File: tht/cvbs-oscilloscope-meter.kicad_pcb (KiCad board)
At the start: 2 copper layers, 50 parts, among them J1 Conn_Coaxial_Power, J2 Conn_Coaxial_Power, J3 Conn_Coaxial_Power, J4 Conn_Coaxial_Power, J5 Barrel_Jack_Switch, J6 Molex 3.96mm, Q1 2N3906, Q2 2N3906, Q3 2N3904, Q4 2N3904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

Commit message: Updated THT
Starting new routing for new schematic layout
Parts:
- C6: footprint Inductor_THT:L_Axial_L11.0mm_D4.5mm_P15.24mm_Horizontal_Fastron_MECC -> Capacitor_THT:C_Disc_D7.5mm_W2.5mm_P5.00mm
- moved U1 91.6 mm to (167.5, 120.3)
- moved U2 33.4 mm to (197.3, 117.2)
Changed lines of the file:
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@@
     )
   )
-  (footprint "Inductor_THT:L_Axial_L11.0mm_D4.5mm_P15.24mm_Horizontal_Fastron_MECC" (layer "F.Cu")
+  (footprint "Capacitor_THT:C_Disc_D7.5mm_W2.5mm_P5.00mm" (layer "F.Cu")
     (at 151.57 102.68)
-    (descr "Inductor, Axial series, Axial, Horizontal, pin pitch=15.24mm, , length*diameter=11*4.5mm^2, Fastron, MECC, http://www.fastrongroup.com/image-show/21/MECC.pdf?type=Complete-DataSheet&productType=series")
-    (tags "Inductor Axial series Axial Horizontal pin pitch 15.24mm  length 11mm diameter 4.5mm Fastron MECC")
-    (property "Sheetfile" "cvbs-oscilloscope-meter.kicad_sch")
-    (property "Sheetname" "")
-    (attr through_hole)
-    (fp_text reference "C6" (at 7.62 -3.37) (layer "F.SilkS")
-      (effects (font (size 1 1) (thickness 0.15)))
-    )
-    (fp_text value "10u" (at 7.62 3.37) (layer "F.Fab")
-      (effects (font (size 1 1) (thickness 0.15)))
-    )
-    (fp_text user "${REFERENCE}" (at 7.62 0) (layer "F.Fab")
-      (effects (font (size 1 1) (thickness 0.15)))
-    )
-    (fp_line (start 13.24 2.37) (end 13.24 -2.37) (layer "F.SilkS") (width 0.12))
-    (fp_line (start 2 2.37) (end 13.24 2.37) (layer "F.SilkS") (width 0.12))
-    (fp_line (start 1.24 0) (end 2 0) (layer "F.SilkS") (width 0.12))
-    (fp_line (start 14 0) (end 13.24 0) (layer "F.SilkS") (width 0.12))
-    (fp_line (start 2 -2.37) (end 2 2.37) (layer "F.SilkS") (width 0.12))
-    (fp_line (start 13.24 -2.37) (end 2 -2.37) (layer "F.SilkS") (width 0.12))
-    (fp_line (start -1.25 2.5) (end 16.5 2.5) (layer "F.CrtYd") (width 0.05))
-    (fp_line (start 16.5 -2.5) (end -1.25 -2.5) (layer "F.CrtYd") (width 0.05))
-    (fp_line (start 16.5 2.5) (end 16.5 -2.5) (layer "F.CrtYd") (width 0.05))
-    (fp_line (start -1.25 -2.5) (end -1.25 2.5) (layer "F.CrtYd") (width 0.05))
-    (fp_line (start 13.12 -2.25) (end 2.12 -2.25) (layer "F.Fab") (width 0.1))
-    (fp_line (start 13.12 2.25) (end 13.12 -2.25) (layer "F.Fab") (width 0.1))
-    (fp_line (start 2.12 2.25) (end 13.12 2.25) (layer "F.Fab") (width 0.1))
-    (fp_line (start 0 0) (end 2.12 0) (layer "F.Fab") (width 0.1))
-    (fp_line (start 2.12 -2.25) (end 2.12 2.25) (layer "F.Fab") (width 0.1))
-    (fp_line (start 15.24 0) (end 13.12 0) (layer "F.Fab") (width 0.1))
+    (descr "C, Disc series, Radial, pin pitch=5.00mm, , diameter*width=7.5*2.5mm^2, Capacitor, http://www.vishay.com/docs/28535/vy2series.pdf")
+    (tags "C Disc series Radial pin pitch 5.00mm  diameter 7.5mm width 2.5mm Capacitor")
+    (property "Sheetfile" "cvbs-oscilloscope-meter.kicad_sch")
+    (property "Sheetname" "")
+    (attr through_hole)
+    (fp_text reference "C6" (at 2.5 -2.5) (layer "F.SilkS")
+      (effects (font (size 1 1) (thickness 0.15)))
+    )
+    (fp_text value "10u" (at 2.5 2.5) (layer "F.Fab")
+      (effects (font (size 1 1) (thickness 0.15)))
+    )
+    (fp_text user "${REFERENCE}" (at 2.5 0) (layer "F.Fab")
+      (effects (font (size 1 1) (thickness 0.15)))
+    )
+    (fp_line (start -1.37 1.37) (end 6.37 1.37) (layer "F.SilkS") (width 0.12))
+    (fp_line (start -1.37 -1.37) (end -1.37 1.37) (layer "F.SilkS") (width 0.12))
+    (fp_line (start 6.37 -1.37) (end 6.37 1.37) (layer "F.SilkS") (width 0.12))
+    (fp_line (start -1.37 -1.37) (end 6.37 -1.37) (layer "F.SilkS") (width 0.12))
+    (fp_line (start 6.5 -1.5) (end -1.5 -1.5) (layer "F.CrtYd") (width 0.05))
+    (fp_line (start -1.5 -1.5) (end -1.5 1.5) (layer "F.CrtYd") (width 0.05))
+    (fp_line (start 6.5 1.5) (end 6.5 -1.5) (layer "F.CrtYd") (width 0.05))
+    (fp_line (start -1.5 1.5) (end 6.5 1.5) (layer "F.CrtYd") (width 0.05))
+    (fp_line (start -1.25 -1.25) (end -1.25 1.25) (layer "F.Fab") (width 0.1))
+    (fp_line (start 6.25 1.25) (end 6.25 -1.25) (layer "F.Fab") (width 0.1))
+    (fp_line (start -1.25 1.25) (end 6.25 1.25) (layer "F.Fab") (width 0.1))
+    (fp_line (start 6.25 -1.25) (end -1.25 -1.25) (layer "F.Fab") (width 0.1))
     (pad "1" thru_hole circle (at 0 0) (size 2 2) (drill 1) (layers *.Cu *.Mask)
       (net 2 "+9V") (pintype "passive"))
-    (pad "2" thru_hole oval (at 15.24 0) (size 2 2) (drill 1) (layers *.Cu *.Mask)
+    (pad "2" thru_hole circle (at 5 0) (size 2 2) (drill 1) (layers *.Cu *.Mask)
       (net 6 "GND") (pintype "passive"))
-    (model "${KICAD6_3DMODEL_DIR}/Inductor_THT.3dshapes/L_Axial_L11.0mm_D4.5mm_P15.24mm_Horizontal_Fastron_MECC.wrl"
+    (model "${KICAD6_3DMODEL_DIR}/Capacitor_THT.3dshapes/C_Disc_D7.5mm_W2.5mm_P5.00mm.wrl"
       (offset (xyz 0 0 0))
       (scale (xyz 1 1 1))
@@
   )
   (footprint "Package_DIP:DIP-8_W7.62mm_Socket_LongPads" (layer "F.Cu")
-    (at 234.5 57.92)
+    (at 167.475 120.33)
     (descr "8-lead though-hole mounted DIP package, row spacing 7.62 mm (300 mils), Socket, LongPads")
     (tags "THT DIP DIL PDIP 2.54mm 7.62mm 300mil Socket LongPads")
@@
   )
   (footprint "Package_DIP:DIP-8_W7.62mm_Socket_LongPads" (layer "F.Cu")
-    (at 202.54 84.12)
+    (at 197.32 117.155)
     (descr "8-lead though-hole mounted DIP package, row spacing 7.62 mm (300 mils), Socket, LongPads")
     (tags "THT DIP DIL PDIP 2.54mm 7.62mm 300mil Socket LongPads")

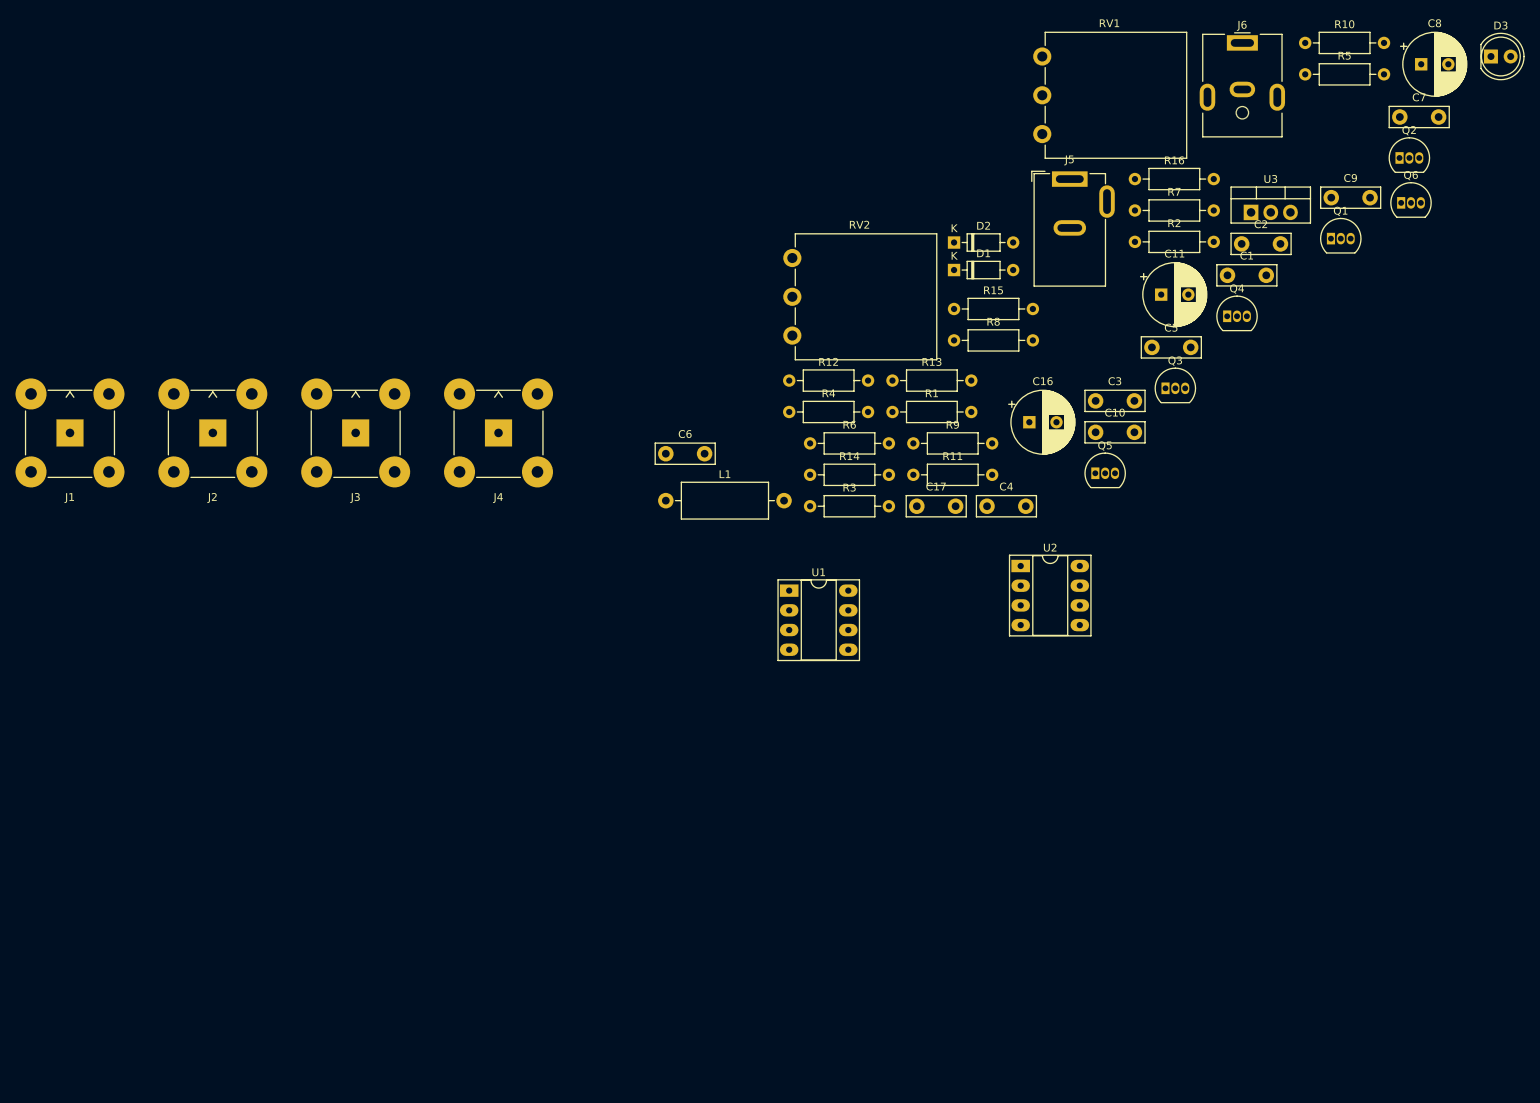
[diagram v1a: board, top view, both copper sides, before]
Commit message: Started PCB layout v2
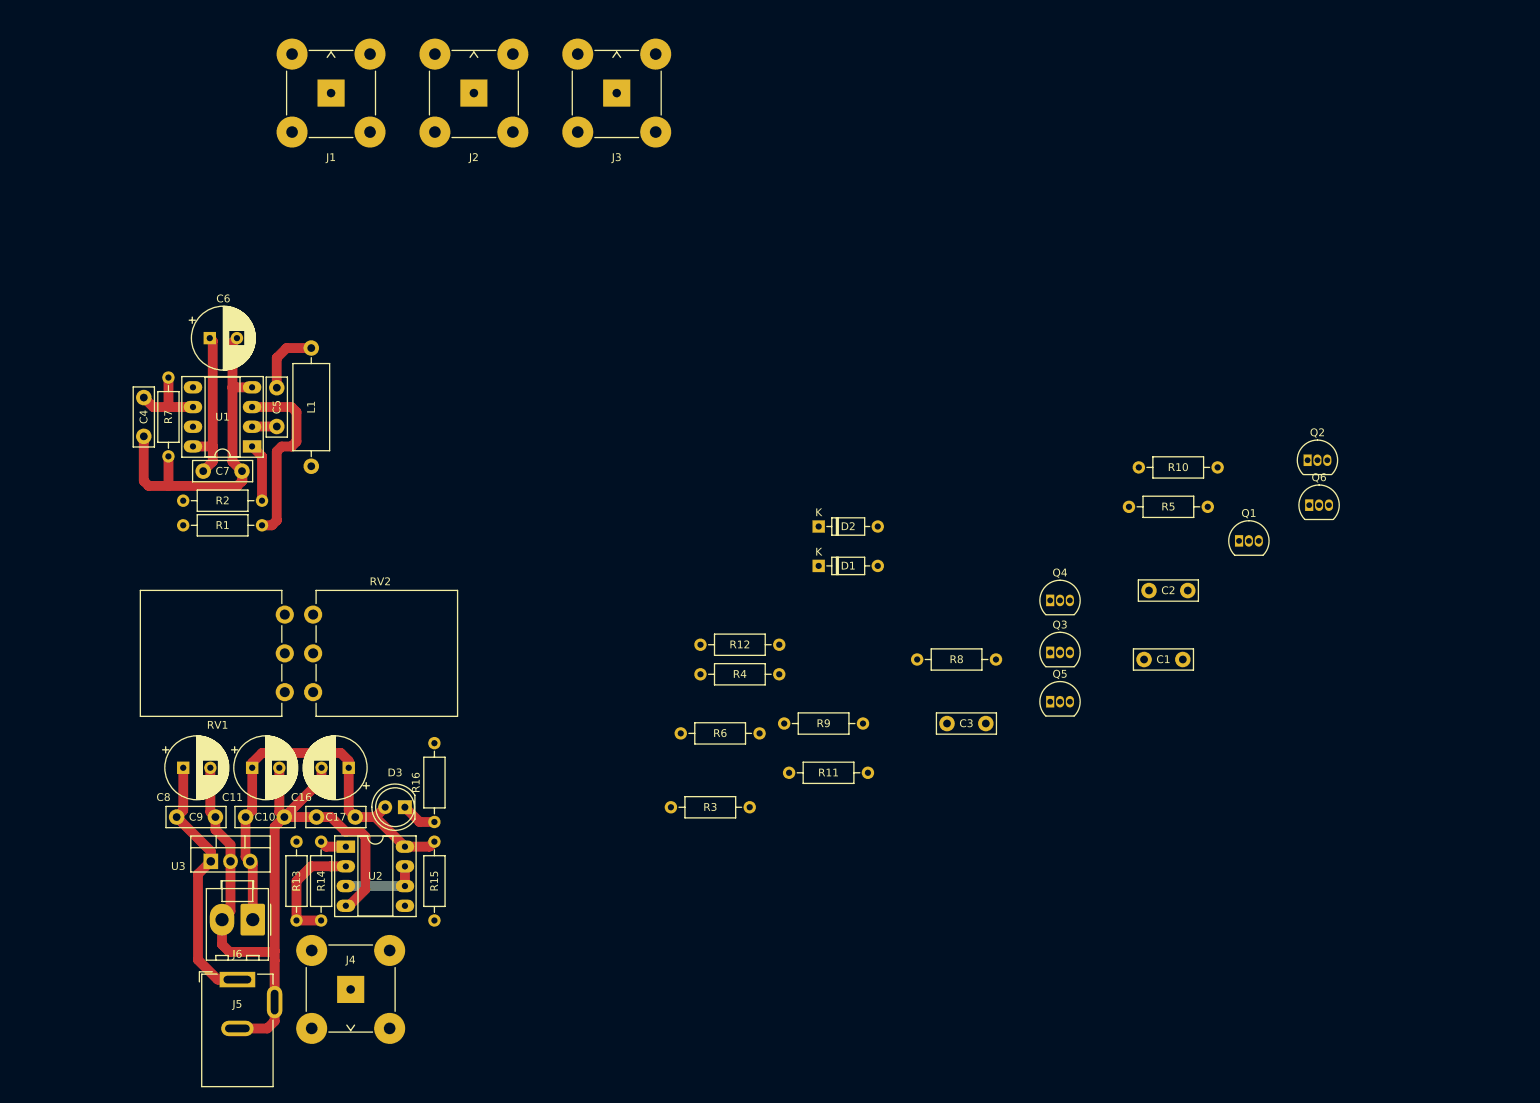
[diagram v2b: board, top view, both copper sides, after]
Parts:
- C6: footprint Capacitor_THT:C_Disc_D7.5mm_W2.5mm_P5.00mm -> Capacitor_THT:CP_Radial_D8.0mm_P3.50mm
- J6: footprint Connector_BarrelJack:BarrelJack_CUI_PJ-063AH_Horizontal -> Connector_Molex:Molex_KK-396_A-41791-0002_1x02_P3.96mm_Vertical
- moved C8 183.6 mm to (89.3, 143.2)
- moved J6 170.5 mm to (98.3, 162.8), turned to 180 degrees
- moved D3 170.2 mm to (117.9, 148.2), turned to 180 degrees
- moved C9 168.9 mm to (88.5, 149.5)
- moved C7 160.9 mm to (91.9, 104.9)
- moved U3 158.1 mm to (92.9, 155.2)
- moved J5 148.9 mm to (96.3, 170.5)
- moved C11 132.1 mm to (98.2, 143.2)
- moved R7 128.6 mm to (87.4, 103.0), turned to 90 degrees
- moved R16 122.6 mm to (121.7, 150.2), turned to 90 degrees
- moved C10 120.3 mm to (97.4, 149.5)
- moved R2 117.4 mm to (99.5, 108.7), turned to 180 degrees
- moved RV1 115.6 mm to (102.4, 123.4), turned to 180 degrees
- moved C5 113.3 mm to (101.4, 99.2), turned to 90 degrees
- moved C4 109.1 mm to (84.3, 100.4), turned to 90 degrees
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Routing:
- net GND: track 0.00 -> 145.6 mm
- net +9V: track 0.00 -> 76.1 mm
- net +VDC: track 0.00 -> 33.8 mm
- net Net-(R1-Pad2): track 0.00 -> 23.9 mm
- net Net-(R13-Pad2): track 0.00 -> 15.4 mm
- net Net-(C4-Pad2): track 0.00 -> 10.7 mm
- net Net-(U2-Pad3): track 0.00 -> 10.2 mm
- net Net-(C5-Pad2): track 0.00 -> 8.82 mm
- net Net-(R2-Pad1): track 0.00 -> 7.53 mm
- net Net-(D3-Pad1): track 0.00 -> 4.59 mm
- net Z: track 0.00 -> 3.45 mm
- net Net-(C5-Pad1): track 0.00 -> 3.20 mm

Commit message: Finished routing
Added routing
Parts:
- moved Q6 107.7 mm to (130.0, 83.4), turned to 180 degrees
- moved Q2 106.9 mm to (127.5, 99.4)
- moved C1 102.7 mm to (117.9, 90.8), turned to -90 degrees
- moved R5 100.4 mm to (114.1, 84.4)
- moved Q1 98.1 mm to (127.5, 109.8)
- moved C2 97.3 mm to (121.1, 90.8), turned to -90 degrees
- moved Q5 82.1 mm to (130.0, 93.6), turned to 180 degrees
- moved Q3 81.5 mm to (130.0, 88.5), turned to 180 degrees
- moved R10 80.5 mm to (133.2, 90.8)
- moved C3 76.0 mm to (124.3, 95.8), turned to 90 degrees
- moved Q4 73.3 mm to (130.0, 103.7), turned to 180 degrees
- moved R11 65.9 mm to (133.2, 87.6)
- moved R4 60.4 mm to (114.1, 87.6)
- moved R8 58.5 mm to (133.2, 100.3)
- moved R3 57.6 mm to (133.2, 93.9)
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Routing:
- net Z: track 3.45 -> 89.5 mm
- net COMP_VIDEO_IN: track 0.00 -> 65.8 mm
- net Net-(RV2-Pad2): track 0.00 -> 57.0 mm
- net Y: track 0.00 -> 48.0 mm
- net GND: track 145.6 -> 100.4 mm
- net Net-(R15-Pad2): track 0.00 -> 43.5 mm
- net +9V: track 76.1 -> 115.6 mm
- net Net-(D1-Pad2): track 0.00 -> 36.1 mm
- net Net-(C2-Pad1): track 0.00 -> 29.9 mm
- net X: track 0.00 -> 28.0 mm
- net Net-(C5-Pad2): track 8.82 -> 34.5 mm
- net Net-(R13-Pad1): track 0.00 -> 23.1 mm
- net Net-(C3-Pad2): track 0.00 -> 16.9 mm
- net Net-(R1-Pad2): track 23.9 -> 8.32 mm
- net Net-(C3-Pad1): track 0.00 -> 13.8 mm
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- added copper zone on B.Cu, net GND
- added copper zone on F.Cu, net GND
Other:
- board outline added: 52.2 x 113.8 mm
